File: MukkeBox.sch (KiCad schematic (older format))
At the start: 50 parts, among them J101 ST_Link_V2_10P, J102 Jumper, J103 Jumper, J104 Jumper, J105 Jumper, J106 Jumper, J107 PinHeader, J108 PinHeader, Q101 NTK3043N, SW101 Rotary_Encoder_Switch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

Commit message: PCB angefangen: Charger geplaced
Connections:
- no-connect marks 3 -> 4
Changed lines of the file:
@@
 Wire Wire Line
 	7950 5900 7450 5900
+NoConn ~ 7450 6000
 $EndSCHEMATC

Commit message: Alle Parts geplaced: Dimension der Platine 200x105qmm. TODO Anzeige überarbeiten
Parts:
- U102: footprint Package_QFP:LQFP-64_10x10mm_P0.5mm -> Package_QFP:LQFP-48_7x7mm_P0.5mm
- Y101: footprint Crystal:Crystal_SMD_HC49-SD_HandSoldering -> Crystal:Crystal_SMD_HC49-SD
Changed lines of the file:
@@
 F 0 "U102" H 6950 6050 50  0000 C CNN
 F 1 "STM32F030C6Tx_MukkeBox" H 6450 5850 50  0000 C CNN
-F 2 "Package_QFP:LQFP-64_10x10mm_P0.5mm" H 4850 2550 50  0001 R CNN
+F 2 "Package_QFP:LQFP-48_7x7mm_P0.5mm" H 4850 2550 50  0001 R CNN
 F 3 "http://www.st.com/st-web-ui/static/active/en/resource/technical/document/datasheet/DM00088500.pdf" H 6050 4650 50  0001 C CNN
 	1    6050 4650
@@
 F 0 "Y101" V 5054 3831 50  0000 L CNN
 F 1 "FOXSDLF/080-20" V 4900 3450 50  0000 L CNN
-F 2 "Crystal:Crystal_SMD_HC49-SD_HandSoldering" H 5100 3700 50  0001 C CNN
+F 2 "Crystal:Crystal_SMD_HC49-SD" H 5100 3700 50  0001 C CNN
 F 3 "~" H 5100 3700 50  0001 C CNN
 	1    5100 3700

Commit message: Mountingholes und Heatsinks hinzugefügt
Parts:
- removed SW101: Rotary_Encoder_Switch, Rotary_Encoder:RotaryEncoder_Alps_EC11E-Switch_Vertical_H20mm_CircularMountingHoles, symbol Device:Rotary_Encoder_Switch
- added H101, H102, H103, H104, H105, H106: MountingHole_Pad, MountingHole:MountingHole_3.2mm_M3_DIN965_Pad, symbol Mechanical:MountingHole_Pad
- added J109: PinHeader, Connector_PinHeader_2.54mm:PinHeader_2x03_P2.54mm_Vertical_SMD, symbol Connector_Generic:Conn_02x03_Counter_Clockwise
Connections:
- wire segments 232 -> 245
- no-connect marks 4 -> 5
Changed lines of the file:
@@
 F1 "Anzeige.sch" 50
 $EndSheet
-$Comp
-L Device:Rotary_Encoder_Switch SW101
-U 1 1 5F64B493
-P 9300 5800
-F 0 "SW101" H 9300 6167 50  0000 C CNN
-F 1 "Rotary_Encoder_Switch" H 9400 6100 50  0000 C CNN
-F 2 "Rotary_Encoder:RotaryEncoder_Alps_EC11E-Switch_Vertical_H20mm_CircularMountingHoles" H 9150 5960 50  0001 C CNN
-F 3 "https://www.mouser.de/datasheet/2/54/PEC12R-777795.pdf" H 9300 6060 50  0001 C CNN
-	1    9300 5800
-	1    0    0    -1
-$EndComp
 Wire Wire Line
 	9000 5700 8400 5700
@@
 Wire Wire Line
 	10000 5550 10000 5700
-Wire Wire Line
-	10000 5700 9600 5700
 Text Label 10100 5700 0    50   ~ 0
 ENC_SW
@@
 	7950 5900 7450 5900
 NoConn ~ 7450 6000
+$Comp
+L Connector_Generic:Conn_02x03_Counter_Clockwise J109
+U 1 1 5E96EE08
+P 9200 5800
+F 0 "J109" H 9250 6000 50  0000 C CNN
+F 1 "PinHeader" H 9250 5550 50  0000 C CNN
+F 2 "Connector_PinHeader_2.54mm:PinHeader_2x03_P2.54mm_Vertical_SMD" H 9200 5800 50  0001 C CNN
+F 3 "~" H 9200 5800 50  0001 C CNN
+	1    9200 5800
+	1    0    0    -1
+$EndComp
+Wire Wire Line
+	9600 5900 9500 5900
+Wire Wire Line
+	9500 5700 10000 5700
+NoConn ~ 9500 5800
+$Comp
+L Mechanical:MountingHole_Pad H101
+U 1 1 5E9D647A
+P 10300 800
+F 0 "H101" V 10254 950 50  0000 L CNN
+F 1 "MountingHole_Pad" V 10345 950 50  0000 L CNN
+F 2 "MountingHole:MountingHole_3.2mm_M3_DIN965_Pad" H 10300 800 50  0001 C CNN
+F 3 "~" H 10300 800 50  0001 C CNN
+	1    10300 800
+	0    1    1    0
+$EndComp
+$Comp
+L Mechanical:MountingHole_Pad H102
+U 1 1 5E9D663C
+P 10300 1000
+F 0 "H102" V 10254 1150 50  0000 L CNN
+F 1 "MountingHole_Pad" V 10345 1150 50  0000 L CNN
+F 2 "MountingHole:MountingHole_3.2mm_M3_DIN965_Pad" H 10300 1000 50  0001 C CNN
+F 3 "~" H 10300 1000 50  0001 C CNN
+	1    10300 1000
+	0    1    1    0
+$EndComp
+$Comp
+L Mechanical:MountingHole_Pad H103
+U 1 1 5E9D66BC
+P 10300 1200
+F 0 "H103" V 10254 1350 50  0000 L CNN
+F 1 "MountingHole_Pad" V 10345 1350 50  0000 L CNN
+F 2 "MountingHole:MountingHole_3.2mm_M3_DIN965_Pad" H 10300 1200 50  0001 C CNN
+F 3 "~" H 10300 1200 50  0001 C CNN
+	1    10300 1200
+	0    1    1    0
+$EndComp
+$Comp
+L Mechanical:MountingHole_Pad H104
+U 1 1 5E9D673A
+P 10300 1400
+F 0 "H104" V 10254 1550 50  0000 L CNN
+F 1 "MountingHole_Pad" V 10345 1550 50  0000 L CNN
+F 2 "MountingHole:MountingHole_3.2mm_M3_DIN965_Pad" H 10300 1400 50  0001 C CNN
+F 3 "~" H 10300 1400 50  0001 C CNN
+	1    10300 1400
+	0    1    1    0
+$EndComp
+$Comp
+L Mechanical:MountingHole_Pad H105
+U 1 1 5E9D6872
+P 10300 1600
+F 0 "H105" V 10254 1750 50  0000 L CNN
+F 1 "MountingHole_Pad" V 10345 1750 50  0000 L CNN
+F 2 "MountingHole:MountingHole_3.2mm_M3_DIN965_Pad" H 10300 1600 50  0001 C CNN
+F 3 "~" H 10300 1600 50  0001 C CNN
+	1    10300 1600
+	0    1    1    0
+$EndComp
+$Comp
+L Mechanical:MountingHole_Pad H106
+U 1 1 5E9D68F4
+P 10300 1800
+F 0 "H106" V 10254 1950 50  0000 L CNN
+F 1 "MountingHole_Pad" V 10345 1950 50  0000 L CNN
+F 2 "MountingHole:MountingHole_3.2mm_M3_DIN965_Pad" H 10300 1800 50  0001 C CNN
+F 3 "~" H 10300 1800 50  0001 C CNN
+	1    10300 1800
+	0    1    1    0
+$EndComp
+$Comp
+L power:GND #PWR0190
+U 1 1 5E9D6DA0
+P 10150 1950
+F 0 "#PWR0190" H 10150 1700 50  0001 C CNN
+F 1 "GND" H 10155 1777 50  0000 C CNN
+F 2 "" H 10150 1950 50  0001 C CNN
+F 3 "" H 10150 1950 50  0001 C CNN
+	1    10150 1950
+	1    0    0    -1
+$EndComp
+Wire Wire Line
+	10200 800  10150 800
+Wire Wire Line
+	10150 800  10150 1000
+Wire Wire Line
+	10200 1800 10150 1800
+Connection ~ 10150 1800
+Wire Wire Line
+	10150 1800 10150 1950
+Wire Wire Line
+	10200 1600 10150 1600
+Connection ~ 10150 1600
+Wire Wire Line
+	10150 1600 10150 1800
+Wire Wire Line
+	10200 1400 10150 1400
+Connection ~ 10150 1400
+Wire Wire Line
+	10150 1400 10150 1600
+Wire Wire Line
+	10200 1200 10150 1200
+Connection ~ 10150 1200
+Wire Wire Line
+	10150 1200 10150 1400
+Wire Wire Line
+	10200 1000 10150 1000
+Connection ~ 10150 1000
+Wire Wire Line
+	10150 1000 10150 1200
 $EndSCHEMATC

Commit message: fertig zum routen
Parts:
- removed J102, J103, J104, J105, J106: Jumper, Connector_PinHeader_2.54mm:PinHeader_1x02_P2.54mm_Vertical, symbol Connector_Generic:Conn_02x01
- added J104: Conn_02x05_Odd_Even, Connector_PinHeader_2.54mm:PinHeader_2x05_P2.54mm_Vertical_SMD, symbol Connector_Generic:Conn_02x05_Odd_Even
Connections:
- net +3V3: now also J104.9 (Pin_9)
- net RxT: now also J104.8 (Pin_8)
- net SCL: now also J104.2 (Pin_2)
- net SDA: now also J104.4 (Pin_4)
- net TxR: now also J104.6 (Pin_6)
- net ST_Link_3V3: now reaches J101.7 (3V3), J101.8 (3V3)
- net ST_Link_3V3: now also J104.10 (Pin_10)
- net at U102.21 (PB10/I2C_SCL): now also J104.1 (Pin_1)
- net at U102.22 (PB11/I2C_SDA): now also J104.3 (Pin_3)
- net at U102.30 (PA9/USART_TX): now also J104.5 (Pin_5)
- net at U102.31 (PA10/USART_RX): now also J104.7 (Pin_7)
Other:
- moved on the sheet: J101
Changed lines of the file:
@@
 L Connector:ST_Link_V2_10P J101
 U 1 1 5E7E5D5D
-P 5100 7000
-F 0 "J101" H 5075 7425 50  0000 C CNN
-F 1 "ST_Link_V2_10P" H 5075 7334 50  0000 C CNN
-F 2 "Connector_PinHeader_2.54mm:PinHeader_2x05_P2.54mm_Vertical" H 5100 7500 50  0001 C CNN
-F 3 "" H 5100 7500 50  0001 C CNN
-	1    5100 7000
+P 5500 7350
+F 0 "J101" H 5475 7775 50  0000 C CNN
+F 1 "ST_Link_V2_10P" H 5475 7684 50  0000 C CNN
+F 2 "Connector_PinHeader_2.54mm:PinHeader_2x05_P2.54mm_Vertical" H 5500 7850 50  0001 C CNN
+F 3 "" H 5500 7850 50  0001 C CNN
+	1    5500 7350
 	1    0    0    -1
 $EndComp
@@
 F1 "Bluetooth.sch" 50
 $EndSheet
-Text GLabel 8750 4450 2    50   Input ~ 0
+Text GLabel 8750 4300 2    50   Input ~ 0
 RxT
-Text GLabel 8750 4350 2    50   Input ~ 0
+Text GLabel 8750 4200 2    50   Input ~ 0
 TxR
 $Comp
@@
 Text Notes 4900 4000 0    50   ~ 0
 ANA_IN
-Text Notes 9000 4050 0    50   ~ 0
+Text Notes 8950 4050 0    50   ~ 0
 GPIO
-Text Notes 9000 4150 0    50   ~ 0
+Text Notes 8950 4150 0    50   ~ 0
 GPIO
-Text Notes 8950 4400 0    50   ~ 0
+Text Notes 8950 4250 0    50   ~ 0
 GPIO
-Text Notes 8950 4500 0    50   ~ 0
+Text Notes 8950 4350 0    50   ~ 0
 GPIO
 Text Notes 3900 5500 0    50   ~ 0
 GPI
-Text Label 5750 6800 0    50   ~ 0
+Text Label 6150 7150 0    50   ~ 0
 SWDIO
-Text Label 5750 7000 0    50   ~ 0
+Text Label 6150 7350 0    50   ~ 0
 SWCLK
 Wire Wire Line
-	5750 7000 5450 7000
-Wire Wire Line
-	5750 6800 5450 6800
-Text Notes 6100 6800 0    50   ~ 0
+	6150 7350 5850 7350
+Wire Wire Line
+	6150 7150 5850 7150
+Text Notes 6500 7150 0    50   ~ 0
 GPIO
-Text Notes 6100 7000 0    50   ~ 0
+Text Notes 6500 7350 0    50   ~ 0
 GPIO
 Text Notes 1550 5650 0    50   ~ 0
@@
 L power:GND #PWR0165
 U 1 1 5EA7CAF7
-P 4450 6900
-F 0 "#PWR0165" H 4450 6650 50  0001 C CNN
-F 1 "GND" V 4455 6727 50  0000 C CNN
-F 2 "" H 4450 6900 50  0001 C CNN
-F 3 "" H 4450 6900 50  0001 C CNN
-	1    4450 6900
-	0    1    1    0
-$EndComp
-Wire Wire Line
-	4700 6900 4450 6900
+P 4850 7250
+F 0 "#PWR0165" H 4850 7000 50  0001 C CNN
+F 1 "GND" V 4855 7077 50  0000 C CNN
+F 2 "" H 4850 7250 50  0001 C CNN
+F 3 "" H 4850 7250 50  0001 C CNN
+	1    4850 7250
+	0    1    1    0
+$EndComp
+Wire Wire Line
+	5100 7250 4850 7250
 $Comp
 L power:GND #PWR0174
 U 1 1 5EA8127F
-P 5750 6900
-F 0 "#PWR0174" H 5750 6650 50  0001 C CNN
-F 1 "GND" V 5755 6727 50  0000 C CNN
-F 2 "" H 5750 6900 50  0001 C CNN
-F 3 "" H 5750 6900 50  0001 C CNN
-	1    5750 6900
+P 6150 7250
+F 0 "#PWR0174" H 6150 7000 50  0001 C CNN
+F 1 "GND" V 6155 7077 50  0000 C CNN
+F 2 "" H 6150 7250 50  0001 C CNN
+F 3 "" H 6150 7250 50  0001 C CNN
+	1    6150 7250
 	0    -1   -1   0
 $EndComp
 Wire Wire Line
-	5750 6900 5450 6900
+	6150 7250 5850 7250
 Text Label 9450 4100 2    50   ~ 0
 BASS
@@
 	1    0    0    -1
 $EndComp
-Text Label 4400 6800 2    50   ~ 0
+Text Label 4800 7150 2    50   ~ 0
 RST
 Wire Wire Line
-	4700 6800 4400 6800
+	5100 7150 4800 7150
 Text Label 5150 3250 2    50   ~ 0
 RST
@@
 Wire Wire Line
 	8750 4800 7450 4800
-$Comp
-L Connector_Generic:Conn_02x01 J103
-U 1 1 5EB922F7
-P 7900 4450
-F 0 "J103" H 7750 4350 50  0000 C CNN
-F 1 "Jumper" H 8100 4350 50  0000 C CNN
-F 2 "Connector_PinHeader_2.54mm:PinHeader_1x02_P2.54mm_Vertical" H 7900 4450 50  0001 C CNN
-F 3 "~" H 7900 4450 50  0001 C CNN
-	1    7900 4450
-	1    0    0    -1
-$EndComp
-$Comp
-L Connector_Generic:Conn_02x01 J105
-U 1 1 5EBA6EA9
-P 8250 4350
-F 0 "J105" H 8100 4450 50  0000 C CNN
-F 1 "Jumper" H 8500 4450 50  0000 C CNN
-F 2 "Connector_PinHeader_2.54mm:PinHeader_1x02_P2.54mm_Vertical" H 8250 4350 50  0001 C CNN
-F 3 "~" H 8250 4350 50  0001 C CNN
-	1    8250 4350
-	1    0    0    -1
-$EndComp
-Wire Wire Line
-	8750 4350 8550 4350
-Wire Wire Line
-	8750 4450 8200 4450
 Wire Wire Line
 	7700 4450 7450 4450
-Wire Wire Line
-	8050 4350 7450 4350
-$Comp
-L Connector_Generic:Conn_02x01 J104
-U 1 1 5EC070B4
-P 8250 4000
-F 0 "J104" H 8100 4100 50  0000 C CNN
-F 1 "Jumper" H 8500 4100 50  0000 C CNN
-F 2 "Connector_PinHeader_2.54mm:PinHeader_1x02_P2.54mm_Vertical" H 8250 4000 50  0001 C CNN
-F 3 "~" H 8250 4000 50  0001 C CNN
-	1    8250 4000
-	1    0    0    -1
-$EndComp
-$Comp
-L Connector_Generic:Conn_02x01 J102
-U 1 1 5EC07148
-P 7900 4100
-F 0 "J102" H 7750 4000 50  0000 C CNN
-F 1 "Jumper" H 8100 4000 50  0000 C CNN
-F 2 "Connector_PinHeader_2.54mm:PinHeader_1x02_P2.54mm_Vertical" H 7900 4100 50  0001 C CNN
-F 3 "~" H 7900 4100 50  0001 C CNN
-	1    7900 4100
-	1    0    0    -1
-$EndComp
-Wire Wire Line
-	8050 4000 7450 4000
-Wire Wire Line
-	7700 4100 7450 4100
-Wire Wire Line
-	8550 4000 8750 4000
-Wire Wire Line
-	8750 4100 8200 4100
 Wire Wire Line
 	4750 4900 5450 4900
@@
 $EndComp
 Connection ~ 6800 2750
-NoConn ~ 5450 7200
-NoConn ~ 4700 7200
-NoConn ~ 4700 7000
-$Comp
-L Connector_Generic:Conn_02x01 J106
-U 1 1 5EB2E486
-P 4200 7650
-F 0 "J106" H 4050 7750 50  0000 C CNN
-F 1 "Jumper" H 4450 7750 50  0000 C CNN
-F 2 "Connector_PinHeader_2.54mm:PinHeader_1x02_P2.54mm_Vertical" H 4200 7650 50  0001 C CNN
-F 3 "~" H 4200 7650 50  0001 C CNN
-	1    4200 7650
-	1    0    0    -1
-$EndComp
-Wire Wire Line
-	5450 7100 5600 7100
-Wire Wire Line
-	5600 7100 5600 7350
-Wire Wire Line
-	5600 7350 4600 7350
-Wire Wire Line
-	4600 7350 4600 7650
-Wire Wire Line
-	4600 7650 4500 7650
-Wire Wire Line
-	4700 7100 4600 7100
-Wire Wire Line
-	4600 7100 4600 7350
-Connection ~ 4600 7350
+NoConn ~ 5850 7550
+NoConn ~ 5100 7550
+NoConn ~ 5100 7350
+Wire Wire Line
+	5850 7450 6000 7450
+Wire Wire Line
+	6000 7450 6000 7700
+Wire Wire Line
+	6000 7700 5000 7700
+Wire Wire Line
+	5100 7450 5000 7450
+Wire Wire Line
+	5000 7450 5000 7700
 $Comp
 L power:+3.3V #PWR0177
 U 1 1 5EB4E6E4
-P 3850 7650
-F 0 "#PWR0177" H 3850 7500 50  0001 C CNN
-F 1 "+3.3V" H 3865 7823 50  0000 C CNN
-F 2 "" H 3850 7650 50  0001 C CNN
-F 3 "" H 3850 7650 50  0001 C CNN
-	1    3850 7650
-	1    0    0    -1
-$EndComp
-Wire Wire Line
-	4000 7650 3850 7650
+P 7950 4400
+F 0 "#PWR0177" H 7950 4250 50  0001 C CNN
+F 1 "+3.3V" V 7850 4400 50  0000 C CNN
+F 2 "" H 7950 4400 50  0001 C CNN
+F 3 "" H 7950 4400 50  0001 C CNN
+	1    7950 4400
+	0    -1   -1   0
+$EndComp
 $Comp
 L power:PWR_FLAG #FLG0101
@@
 Wire Wire Line
 	10150 1000 10150 1200
+Wire Wire Line
+	8750 4100 8450 4100
+Wire Wire Line
+	8450 4200 8750 4200
+Wire Wire Line
+	8450 4300 8750 4300
+Wire Wire Line
+	8450 4000 8750 4000
+Wire Wire Line
+	7950 4000 7450 4000
+Wire Wire Line
+	7450 4100 7950 4100
+Wire Wire Line
+	7950 4200 7600 4200
+Wire Wire Line
+	7600 4200 7600 4350
+Wire Wire Line
+	7600 4350 7450 4350
+Wire Wire Line
+	7950 4300 7700 4300
+Wire Wire Line
+	7700 4300 7700 4450
+Text Label 8450 4400 0    50   ~ 0
+ST_Link_3V3
+Text Label 5250 7700 0    50   ~ 0
+ST_Link_3V3
+$Comp
+L Connector_Generic:Conn_02x05_Odd_Even J104
+U 1 1 5EAA894B
+P 8150 4200
+F 0 "J104" H 8200 4617 50  0000 C CNN
+F 1 "Conn_02x05_Odd_Even" H 8200 4526 50  0000 C CNN
+F 2 "Connector_PinHeader_2.54mm:PinHeader_2x05_P2.54mm_Vertical_SMD" H 8150 4200 50  0001 C CNN
+F 3 "~" H 8150 4200 50  0001 C CNN
+	1    8150 4200
+	1    0    0    -1
+$EndComp
 $EndSCHEMATC

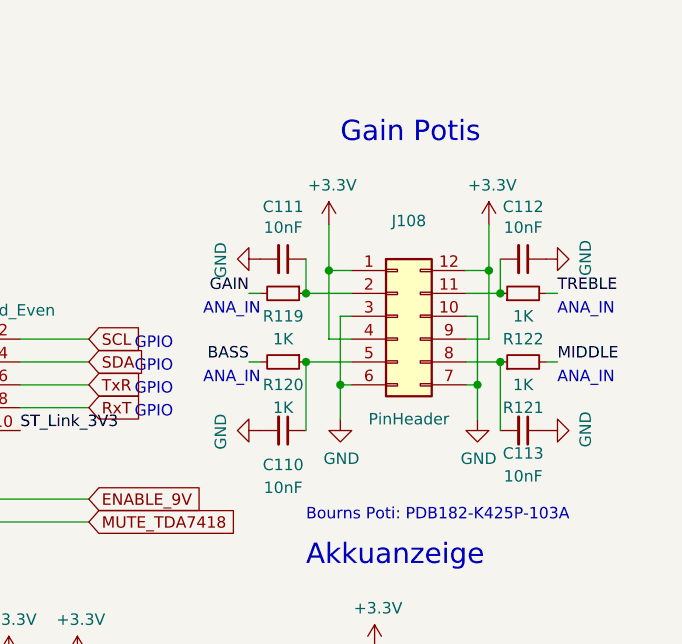
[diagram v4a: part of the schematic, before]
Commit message: Folienkondensatoren SMD gegen THT ausgetauscht. Kleine Fehler korrigiert
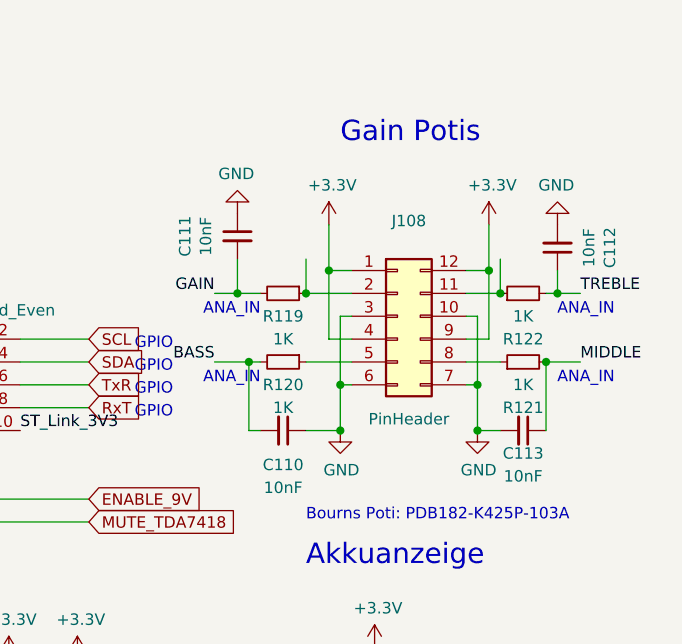
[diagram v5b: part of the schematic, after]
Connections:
- net BASS: now also C110.2
- net GAIN: now also C111.2
- net GND: now also C110.1, C111.1, C112.2, C113.2; no longer C110.2, C111.2, C112.1, C113.1
- net MIDDLE: now also C113.1
- net TREBLE: now also C112.1
- net at J108.5 (Pin_5), R120.1: no longer C110.1
- net at J108.2 (Pin_2), R119.1: no longer C111.1
- net at J108.11 (Pin_11), R122.1: no longer C112.2
- net at J108.8 (Pin_8), R121.1: no longer C113.2
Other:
- moved on the sheet: C111, C112
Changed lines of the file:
@@
 Wire Wire Line
 	6150 7250 5850 7250
-Text Label 9450 4100 2    50   ~ 0
+Text Label 9300 4100 2    50   ~ 0
 BASS
-Text Label 10800 4100 0    50   ~ 0
+Text Label 10900 4100 0    50   ~ 0
 MIDDLE
-Text Label 10800 3800 0    50   ~ 0
+Text Label 10900 3800 0    50   ~ 0
 TREBLE
-Text Label 9450 3800 2    50   ~ 0
+Text Label 9300 3800 2    50   ~ 0
 GAIN
 Text Notes 9250 3900 0    50   ~ 0
@@
 L Device:C_Small C111
 U 1 1 5EAA9E05
-P 9600 3650
-F 0 "C111" V 9371 3650 50  0000 C CNN
-F 1 "10nF" V 9462 3650 50  0000 C CNN
-F 2 "Capacitor_SMD:C_0603_1608Metric_Pad1.05x0.95mm_HandSolder" H 9600 3650 50  0001 C CNN
-F 3 "~" H 9600 3650 50  0001 C CNN
-	1    9600 3650
-	0    1    1    0
+P 9400 3550
+F 0 "C111" V 9171 3550 50  0000 C CNN
+F 1 "10nF" V 9262 3550 50  0000 C CNN
+F 2 "Capacitor_SMD:C_0603_1608Metric_Pad1.05x0.95mm_HandSolder" H 9400 3550 50  0001 C CNN
+F 3 "~" H 9400 3550 50  0001 C CNN
+	1    9400 3550
+	1    0    0    -1
 $EndComp
 $Comp
 L Device:C_Small C112
 U 1 1 5EAA9E8D
-P 10650 3650
-F 0 "C112" V 10421 3650 50  0000 C CNN
-F 1 "10nF" V 10512 3650 50  0000 C CNN
-F 2 "Capacitor_SMD:C_0603_1608Metric_Pad1.05x0.95mm_HandSolder" H 10650 3650 50  0001 C CNN
-F 3 "~" H 10650 3650 50  0001 C CNN
-	1    10650 3650
-	0    1    1    0
+P 10800 3600
+F 0 "C112" V 10571 3600 50  0000 C CNN
+F 1 "10nF" V 10662 3600 50  0000 C CNN
+F 2 "Capacitor_SMD:C_0603_1608Metric_Pad1.05x0.95mm_HandSolder" H 10800 3600 50  0001 C CNN
+F 3 "~" H 10800 3600 50  0001 C CNN
+	1    10800 3600
+	-1   0    0    1
 $EndComp
 $Comp
@@
 $EndComp
 Wire Wire Line
-	9500 3800 9450 3800
+	9500 3800 9400 3800
 Wire Wire Line
 	9500 4100 9450 4100
-Wire Wire Line
-	10750 4100 10800 4100
 Wire Wire Line
 	10750 3800 10800 3800
@@
 L power:GND #PWR0182
 U 1 1 5F17A631
-P 10450 4350
-F 0 "#PWR0182" H 10450 4100 50  0001 C CNN
-F 1 "GND" H 10455 4177 50  0000 C CNN
-F 2 "" H 10450 4350 50  0001 C CNN
-F 3 "" H 10450 4350 50  0001 C CNN
-	1    10450 4350
-	1    0    0    -1
-$EndComp
-Wire Wire Line
-	10450 4350 10450 4200
+P 10450 4400
+F 0 "#PWR0182" H 10450 4150 50  0001 C CNN
+F 1 "GND" H 10455 4227 50  0000 C CNN
+F 2 "" H 10450 4400 50  0001 C CNN
+F 3 "" H 10450 4400 50  0001 C CNN
+	1    10450 4400
+	1    0    0    -1
+$EndComp
 Wire Wire Line
 	10450 4200 10400 4200
@@
 L power:GND #PWR0181
 U 1 1 5F1AAEE8
-P 9850 4350
-F 0 "#PWR0181" H 9850 4100 50  0001 C CNN
-F 1 "GND" H 9855 4177 50  0000 C CNN
-F 2 "" H 9850 4350 50  0001 C CNN
-F 3 "" H 9850 4350 50  0001 C CNN
-	1    9850 4350
+P 9850 4400
+F 0 "#PWR0181" H 9850 4150 50  0001 C CNN
+F 1 "GND" H 9855 4227 50  0000 C CNN
+F 2 "" H 9850 4400 50  0001 C CNN
+F 3 "" H 9850 4400 50  0001 C CNN
+	1    9850 4400
 	1    0    0    -1
 $EndComp
 Wire Wire Line
 	9900 4200 9850 4200
-Wire Wire Line
-	9850 4200 9850 4350
 Wire Wire Line
 	9900 3900 9850 3900
@@
 Connection ~ 9850 4200
 Wire Wire Line
-	9700 4400 9700 4100
-Connection ~ 9700 4100
-Wire Wire Line
 	9700 3650 9700 3800
 Connection ~ 9700 3800
@@
 	10550 3650 10550 3800
 Connection ~ 10550 3800
-Wire Wire Line
-	10550 4400 10550 4100
-Connection ~ 10550 4100
-$Comp
-L power:GND #PWR0185
-U 1 1 5F529D2D
-P 10750 4400
-F 0 "#PWR0185" H 10750 4150 50  0001 C CNN
-F 1 "GND" H 10755 4227 50  0000 C CNN
-F 2 "" H 10750 4400 50  0001 C CNN
-F 3 "" H 10750 4400 50  0001 C CNN
-	1    10750 4400
-	0    -1   -1   0
-$EndComp
 $Comp
 L power:GND #PWR0184
 U 1 1 5F529E46
-P 10750 3650
-F 0 "#PWR0184" H 10750 3400 50  0001 C CNN
-F 1 "GND" H 10755 3477 50  0000 C CNN
-F 2 "" H 10750 3650 50  0001 C CNN
-F 3 "" H 10750 3650 50  0001 C CNN
-	1    10750 3650
-	0    -1   -1   0
+P 10800 3500
+F 0 "#PWR0184" H 10800 3250 50  0001 C CNN
+F 1 "GND" H 10805 3327 50  0000 C CNN
+F 2 "" H 10800 3500 50  0001 C CNN
+F 3 "" H 10800 3500 50  0001 C CNN
+	1    10800 3500
+	-1   0    0    1
 $EndComp
 $Comp
 L power:GND #PWR0175
 U 1 1 5F529EBD
-P 9500 3650
-F 0 "#PWR0175" H 9500 3400 50  0001 C CNN
-F 1 "GND" H 9505 3477 50  0000 C CNN
-F 2 "" H 9500 3650 50  0001 C CNN
-F 3 "" H 9500 3650 50  0001 C CNN
-	1    9500 3650
-	0    1    1    0
-$EndComp
-$Comp
-L power:GND #PWR0180
-U 1 1 5F529FA0
-P 9500 4400
-F 0 "#PWR0180" H 9500 4150 50  0001 C CNN
-F 1 "GND" H 9505 4227 50  0000 C CNN
-F 2 "" H 9500 4400 50  0001 C CNN
-F 3 "" H 9500 4400 50  0001 C CNN
-	1    9500 4400
-	0    1    1    0
+P 9400 3450
+F 0 "#PWR0175" H 9400 3200 50  0001 C CNN
+F 1 "GND" H 9405 3277 50  0000 C CNN
+F 2 "" H 9400 3450 50  0001 C CNN
+F 3 "" H 9400 3450 50  0001 C CNN
+	1    9400 3450
+	-1   0    0    1
 $EndComp
 $Sheet
@@
 	1    0    0    -1
 $EndComp
+Wire Wire Line
+	9500 4400 9450 4400
+Wire Wire Line
+	9450 4400 9450 4100
+Wire Wire Line
+	9700 4400 9850 4400
+Wire Wire Line
+	9850 4200 9850 4400
+Connection ~ 9850 4400
+Wire Wire Line
+	10750 4400 10750 4100
+Connection ~ 10750 4100
+Wire Wire Line
+	10550 4400 10450 4400
+Wire Wire Line
+	10450 4200 10450 4400
+Connection ~ 10450 4400
+Connection ~ 9450 4100
+Wire Wire Line
+	9400 3650 9400 3800
+Connection ~ 9400 3800
+Wire Wire Line
+	9400 3800 9300 3800
+Wire Wire Line
+	10800 3700 10800 3800
+Wire Wire Line
+	10900 3800 10800 3800
+Connection ~ 10800 3800
+Wire Wire Line
+	10750 4100 10900 4100
+Wire Wire Line
+	9300 4100 9450 4100
 $EndSCHEMATC
